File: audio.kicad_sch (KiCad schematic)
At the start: 4 parts, among them Q3 BC817-25-QVL

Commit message: Add company name (using github URL), date, and change revision number to all schematic pages
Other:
- company: (none) -> github.com/fuad1502/open-running-watch-hw
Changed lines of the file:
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@@
 	(title_block
 		(title "Open Running Watch")
-		(rev "A")
+		(date "2024-04-12")
+		(rev "0.1.0")
+		(company "github.com/fuad1502/open-running-watch-hw")
 	)
 	(junction

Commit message: Changed hand soldered footprints to normal footprints
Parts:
- R49: footprint Resistor_SMD:R_0402_1005Metric_Pad0.72x0.64mm_HandSolder -> Resistor_SMD:R_0402_1005Metric
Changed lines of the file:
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@@
 			)
 		)
-		(property "Footprint" "Resistor_SMD:R_0402_1005Metric_Pad0.72x0.64mm_HandSolder"
+		(property "Footprint" "Resistor_SMD:R_0402_1005Metric"
 			(at 140.97 116.078 90)
 			(effects

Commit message: Remove additional spaces in Manufacturer_Part_Number field
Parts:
- R49: Manufacturer_Part_Number RC0402JR-07240RL -> RC0402JR-07240RL
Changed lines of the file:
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@@
 			)
 		)
-		(property "Manufacturer_Part_Number" "RC0402JR-07240RL "
+		(property "Manufacturer_Part_Number" "RC0402JR-07240RL"
 			(at 140.97 114.3 90)
 			(effects

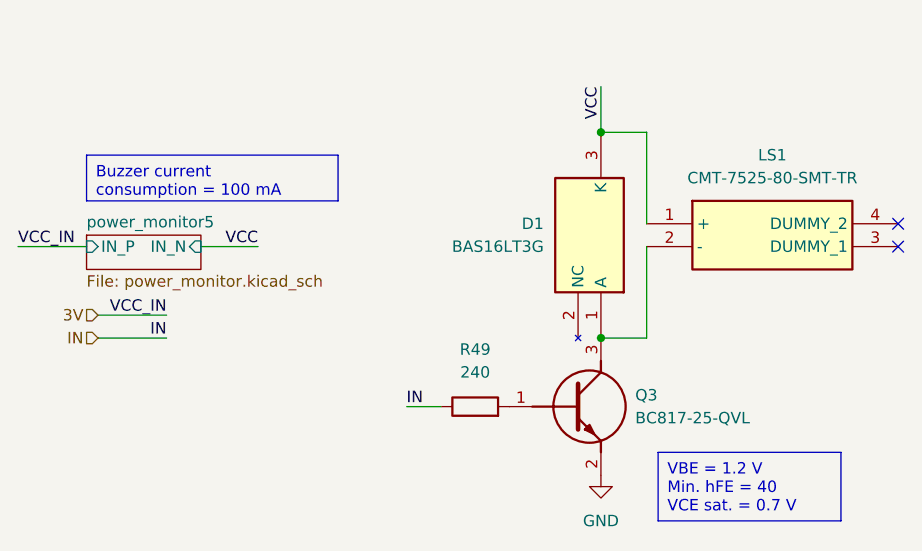
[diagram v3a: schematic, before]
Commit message: Use NPN NMOS pair to switch the piezo on and off, to support higher current handling
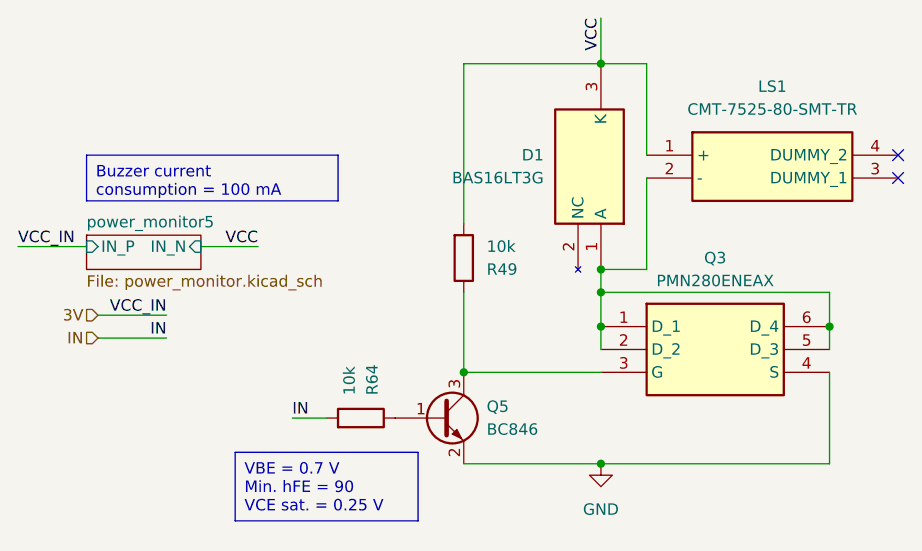
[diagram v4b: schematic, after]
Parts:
- removed Q3: BC817-25-QVL, BC817-25-QVL:SOT95P230X110-3N, symbol BC817-25-QVL:BC817-25-QVL
- added Q3: PMN280ENEAX, PMN280ENEAX:PMN280ENEAX, symbol PMN280ENEAX:PMN280ENEAX
- added Q5: BC846, Package_TO_SOT_SMD:SOT-23, symbol Transistor_BJT:BC846
- added R64: 10k, Resistor_SMD:R_0402_1005Metric, symbol Device:R
- R49: value 240 -> 10k; Manufacturer_Part_Number RC0402JR-07240RL -> RC0402JR-0710KP
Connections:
- net GND: now also Q3.4 (S), Q5.2 (E)
- net IN: now also R64.2; no longer R49.1
- net VCC: now also R49.2
- net at D1.1 (A), LS1.2 (-): now also Q3.1 (D_1), Q3.2 (D_2), Q3.5 (D_3), Q3.6 (D_4)
- new net: Q5.1 (B), R64.1
- new net: Q3.3 (G), Q5.3 (C), R49.1
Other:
- moved on the sheet: D1, LS1
